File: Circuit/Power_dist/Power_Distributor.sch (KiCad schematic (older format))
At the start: 4 parts, among them CON1 Conn-PCIE-x16, J1 Thruster_Off_Switch

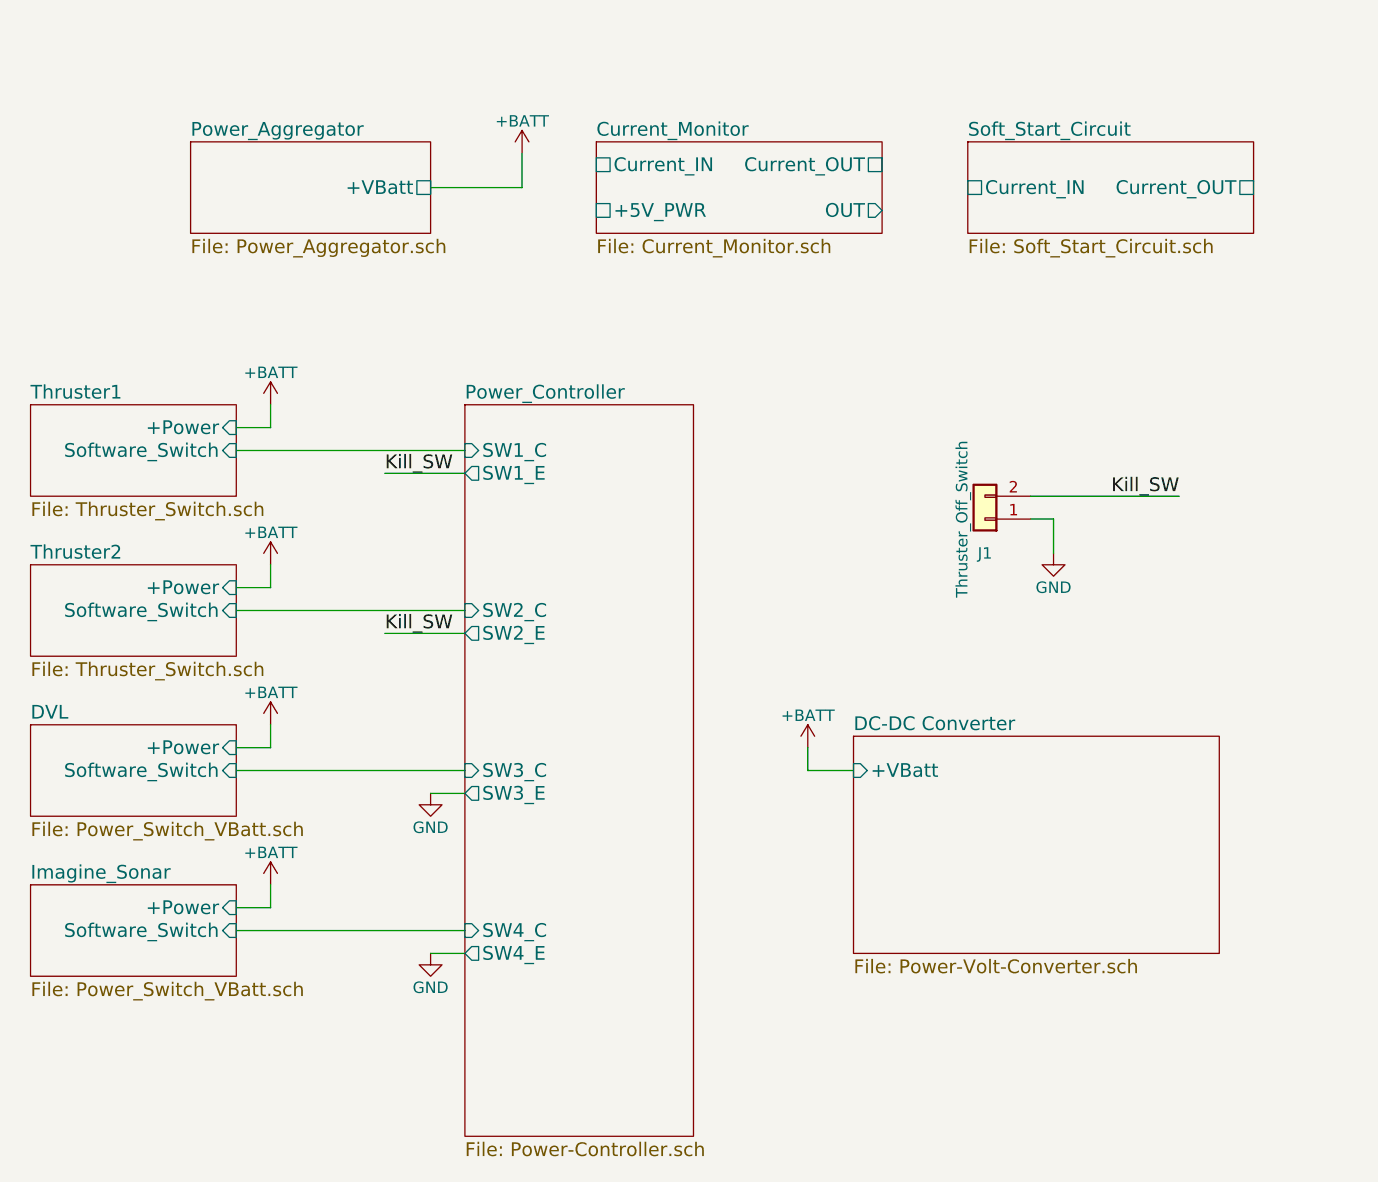
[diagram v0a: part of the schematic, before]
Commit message: added filter to dc-dc converters in Power_dist
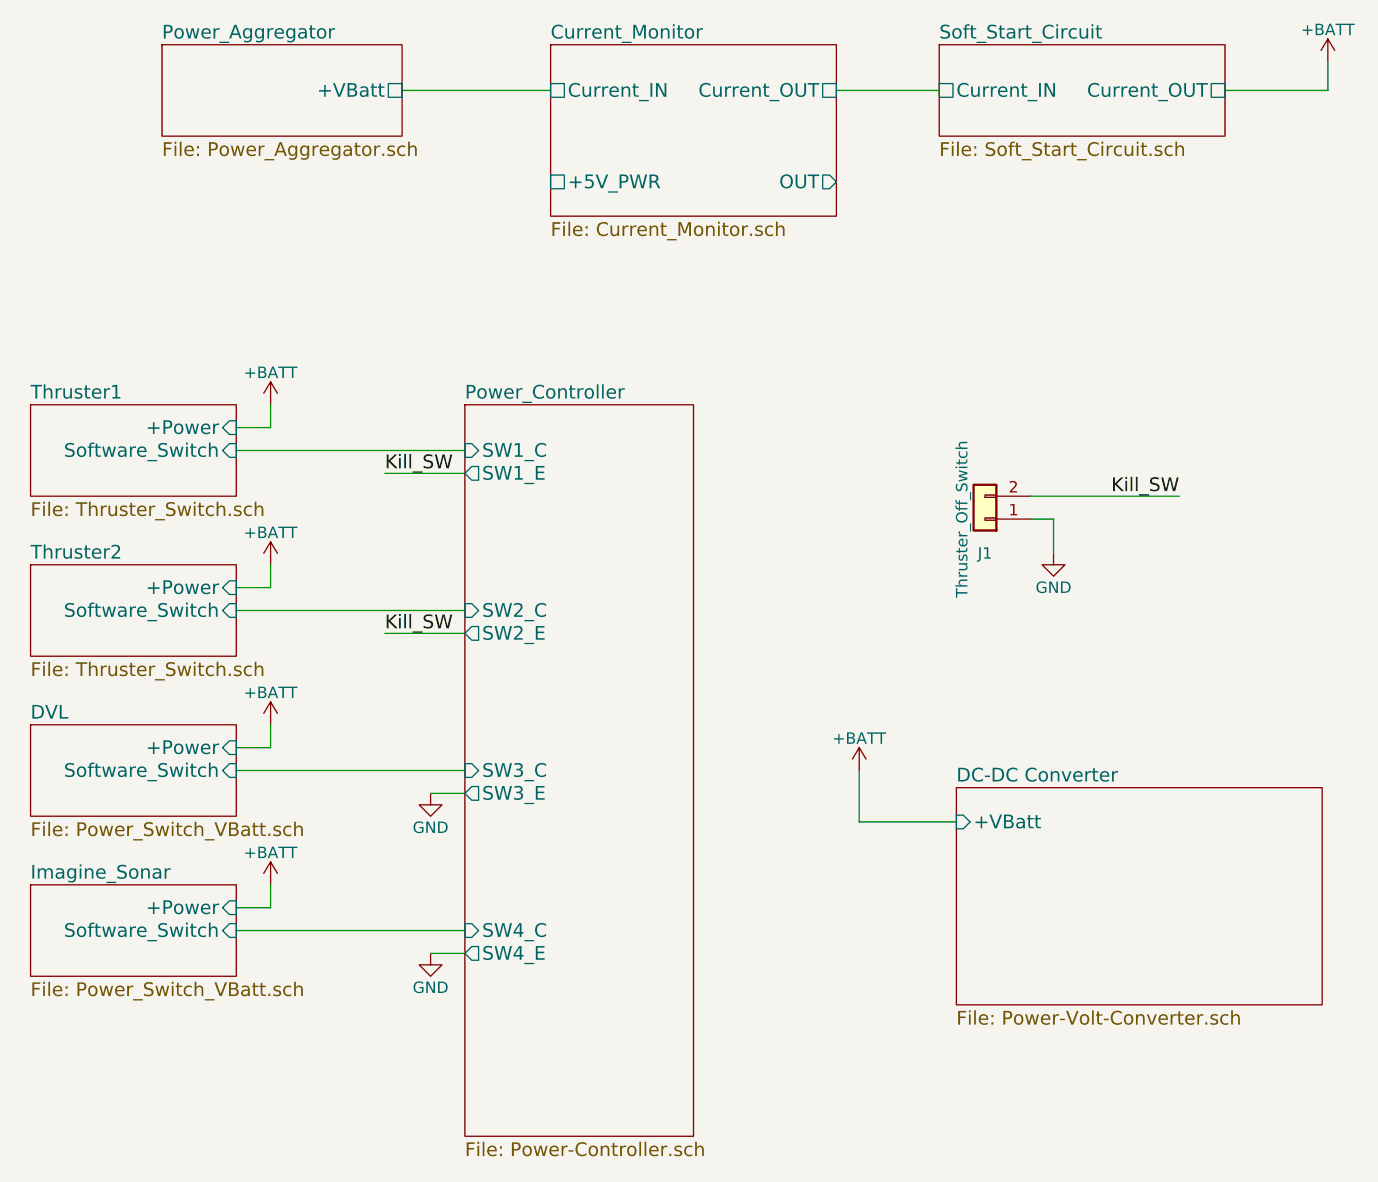
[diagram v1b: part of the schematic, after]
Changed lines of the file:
@@
 L +BATT #PWR01
 U 1 1 58E61C00
-P 6700 1450
-F 0 "#PWR01" H 6700 1300 50  0001 C CNN
-F 1 "+BATT" H 6700 1590 50  0000 C CNN
-F 2 "" H 6700 1450 50  0001 C CNN
-F 3 "" H 6700 1450 50  0001 C CNN
-	1    6700 1450
+P 10225 1050
+F 0 "#PWR01" H 10225 900 50  0001 C CNN
+F 1 "+BATT" H 10225 1190 50  0000 C CNN
+F 2 "" H 10225 1050 50  0001 C CNN
+F 3 "" H 10225 1050 50  0001 C CNN
+	1    10225 1050
 	1    0    0    -1
 $EndComp
@@
 $EndComp
 $Sheet
-S 5250 1400 1050 400
-U 58E5E8B2
-F0 "Power_Aggregator" 60
-F1 "Power_Aggregator.sch" 60
-F2 "+VBatt" U R 6300 1600 60
-$EndSheet
-$Sheet
-S 8150 4000 1600 950
+S 8600 4225 1600 950
 U 58E63E65
 F0 "DC-DC Converter" 60
 F1 "Power-Volt-Converter.sch" 60
-F2 "+VBatt" I L 8150 4150 60
+F2 "+VBatt" I L 8600 4375 60
 $EndSheet
 $Comp
 L +BATT #PWR07
 U 1 1 58E67F6C
-P 7950 4050
-F 0 "#PWR07" H 7950 3900 50  0001 C CNN
-F 1 "+BATT" H 7950 4190 50  0000 C CNN
-F 2 "" H 7950 4050 50  0001 C CNN
-F 3 "" H 7950 4050 50  0001 C CNN
-	1    7950 4050
+P 8175 4150
+F 0 "#PWR07" H 8175 4000 50  0001 C CNN
+F 1 "+BATT" H 8175 4290 50  0000 C CNN
+F 2 "" H 8175 4150 50  0001 C CNN
+F 3 "" H 8175 4150 50  0001 C CNN
+	1    8175 4150
 	1    0    0    -1
 $EndComp
@@
 Wire Wire Line
 	5600 4750 5600 4650
-Wire Wire Line
-	6300 1600 6700 1600
-Wire Wire Line
-	6700 1600 6700 1450
-Wire Wire Line
-	8150 4150 7950 4150
-Wire Wire Line
-	7950 4150 7950 4050
 Wire Wire Line
 	5450 4850 6450 4850
@@
 $EndSheet
 $Sheet
-S 7025 1400 1250 400
+S 6825 975  1250 750
 U 5B4C0CAC
 F0 "Current_Monitor" 60
 F1 "Current_Monitor.sch" 60
-F2 "Current_IN" U L 7025 1500 60
-F3 "Current_OUT" U R 8275 1500 60
-F4 "OUT" O R 8275 1700 60
-F5 "+5V_PWR" U L 7025 1700 60
+F2 "Current_IN" U L 6825 1175 60
+F3 "Current_OUT" U R 8075 1175 60
+F4 "OUT" O R 8075 1575 60
+F5 "+5V_PWR" U L 6825 1575 60
 $EndSheet
 $Sheet
-S 8650 1400 1250 400
+S 8525 975  1250 400
 U 5B4C624E
 F0 "Soft_Start_Circuit" 60
 F1 "Soft_Start_Circuit.sch" 60
-F2 "Current_IN" U L 8650 1600 60
-F3 "Current_OUT" U R 9900 1600 60
+F2 "Current_IN" U L 8525 1175 60
+F3 "Current_OUT" U R 9775 1175 60
 $EndSheet
+$Sheet
+S 5125 975  1050 400
+U 58E5E8B2
+F0 "Power_Aggregator" 60
+F1 "Power_Aggregator.sch" 60
+F2 "+VBatt" U R 6175 1175 60
+$EndSheet
+Wire Wire Line
+	6825 1175 6175 1175
+Wire Wire Line
+	8075 1175 8525 1175
+Wire Wire Line
+	9775 1175 10225 1175
+Wire Wire Line
+	10225 1175 10225 1050
+Wire Wire Line
+	8175 4375 8600 4375
+Wire Wire Line
+	8175 4375 8175 4150
 $EndSCHEMATC

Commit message: added +5v voltage regulator on battery side of Power_dist
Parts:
- added C?: 0.33uF, symbol C_Small
- added C?: 0.1uF, symbol C_Small
- added R?: 0, symbol R
- added U?: L78L05_SOT89, TO_SOT_Packages_SMD:SOT89-3_Housing, symbol L78L05_SOT89
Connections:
- net labels added: +5VP
- wire segments 57 -> 74
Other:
- moved on the sheet: J1
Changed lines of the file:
@@
 L +BATT #PWR01
 U 1 1 58E61C00
-P 10225 1050
-F 0 "#PWR01" H 10225 900 50  0001 C CNN
-F 1 "+BATT" H 10225 1190 50  0000 C CNN
-F 2 "" H 10225 1050 50  0001 C CNN
-F 3 "" H 10225 1050 50  0001 C CNN
-	1    10225 1050
+P 10075 1025
+F 0 "#PWR01" H 10075 875 50  0001 C CNN
+F 1 "+BATT" H 10075 1165 50  0000 C CNN
+F 2 "" H 10075 1025 50  0001 C CNN
+F 3 "" H 10075 1025 50  0001 C CNN
+	1    10075 1025
 	1    0    0    -1
 $EndComp
@@
 L Conn_01x02 J1
 U 1 1 58E6ABEA
-P 8725 3050
-F 0 "J1" H 8725 3200 50  0000 C CNN
-F 1 "Thruster_Off_Switch" V 8825 3050 50  0000 C CNN
-F 2 "Pin_Headers:Pin_Header_Straight_1x02_Pitch2.54mm" H 8725 3050 50  0001 C CNN
-F 3 "" H 8725 3050 50  0001 C CNN
-	1    8725 3050
+P 8725 3225
+F 0 "J1" H 8725 3375 50  0000 C CNN
+F 1 "Thruster_Off_Switch" V 8825 3225 50  0000 C CNN
+F 2 "Pin_Headers:Pin_Header_Straight_1x02_Pitch2.54mm" H 8725 3225 50  0001 C CNN
+F 3 "" H 8725 3225 50  0001 C CNN
+	1    8725 3225
 	-1   0    0    1
 $EndComp
-Text Label 9575 2950 2    60   ~ 0
+Text Label 9575 3125 2    60   ~ 0
 Kill_SW
 $Comp
 L GND #PWR02
 U 1 1 58E6E6F3
-P 9025 3200
-F 0 "#PWR02" H 9025 2950 50  0001 C CNN
-F 1 "GND" H 9025 3050 50  0000 C CNN
-F 2 "" H 9025 3200 50  0001 C CNN
-F 3 "" H 9025 3200 50  0001 C CNN
-	1    9025 3200
+P 9025 3375
+F 0 "#PWR02" H 9025 3125 50  0001 C CNN
+F 1 "GND" H 9025 3225 50  0000 C CNN
+F 2 "" H 9025 3375 50  0001 C CNN
+F 3 "" H 9025 3375 50  0001 C CNN
+	1    9025 3375
 	1    0    0    -1
 $EndComp
@@
 F0 "DC-DC Converter" 60
 F1 "Power-Volt-Converter.sch" 60
-F2 "+VBatt" I L 8600 4375 60
+F2 "+VBatt" U L 8600 4375 60
+F3 "+12V" U L 8600 4850 60
+F4 "+5V" U L 8600 5000 60
 $EndSheet
 $Comp
@@
 	1    0    0    -1
 $EndComp
-Wire Wire Line
-	8925 3050 9025 3050
-Wire Wire Line
-	9025 3050 9025 3200
-Wire Wire Line
-	9575 2950 8925 2950
-Wire Wire Line
-	5600 2550 5600 2650
-Wire Wire Line
-	5600 2650 5450 2650
-Wire Wire Line
-	5600 3250 5600 3350
-Wire Wire Line
-	5600 3350 5450 3350
-Wire Wire Line
-	5600 3950 5600 4050
-Wire Wire Line
-	5600 4050 5450 4050
-Wire Wire Line
-	5450 4750 5600 4750
-Wire Wire Line
-	5600 4750 5600 4650
-Wire Wire Line
-	5450 4850 6450 4850
-Wire Wire Line
-	6450 4150 5450 4150
-Wire Wire Line
-	5450 3450 6450 3450
-Wire Wire Line
-	6450 2750 5450 2750
-Wire Wire Line
-	6100 2850 6450 2850
-Wire Wire Line
-	6100 3550 6450 3550
-Wire Wire Line
-	6300 4250 6450 4250
-Wire Wire Line
-	6450 4950 6300 4950
-Wire Wire Line
-	1950 2750 1450 2750
-Wire Wire Line
-	1950 2650 1450 2650
-Wire Wire Line
-	650  2150 1950 2150
-Wire Wire Line
-	3500 2150 3100 2150
-Wire Wire Line
-	3500 2050 3500 2150
-Wire Wire Line
-	3100 2050 3500 2050
-Connection ~ 3500 2050
-Wire Wire Line
-	1950 1950 1450 1950
-Wire Wire Line
-	1450 1950 1450 1900
-Wire Wire Line
-	1450 1450 1950 1450
-Wire Wire Line
-	1450 1150 1450 1450
-Wire Wire Line
-	1950 1250 1450 1250
-Connection ~ 1450 1250
-Wire Wire Line
-	1950 1350 1450 1350
-Connection ~ 1450 1350
 $Comp
 L +12V #PWR013
@@
 	1    0    0    -1
 $EndComp
-Wire Wire Line
-	1850 1850 1950 1850
 $Comp
 L GNDD #PWR015
@@
 	1    0    0    -1
 $EndComp
-Wire Wire Line
-	1050 1550 1950 1550
-Wire Wire Line
-	3100 1350 3500 1350
-Wire Wire Line
-	3500 1350 3500 1250
-Wire Wire Line
-	3100 1450 3900 1450
-Wire Wire Line
-	3900 1450 3900 1250
 $Comp
 L +BATT #PWR017
@@
 	1    0    0    -1
 $EndComp
-Wire Wire Line
-	1850 1850 1850 1650
-Wire Wire Line
-	1850 1650 1650 1650
-Wire Wire Line
-	1650 1650 1650 1700
 $Comp
 L GND #PWR018
@@
 	1    0    0    -1
 $EndComp
-Wire Wire Line
-	1950 2850 1450 2850
-Wire Wire Line
-	1450 2850 1450 2900
 $Comp
 L GNDREF #PWR019
@@
 	1    0    0    -1
 $EndComp
-Wire Wire Line
-	1950 2550 1050 2550
-Wire Wire Line
-	1950 3050 1050 3050
-Wire Wire Line
-	3100 2450 3500 2450
-Wire Wire Line
-	3100 2750 3500 2750
-Wire Wire Line
-	3500 3050 3100 3050
-Wire Wire Line
-	3500 1550 3100 1550
 $Comp
 L LED_Small D7
@@
 	1    0    0    -1
 $EndComp
-Wire Wire Line
-	800  2250 800  2150
-Connection ~ 800  2150
-Wire Wire Line
-	800  2450 800  2550
-Wire Wire Line
-	800  2850 800  2950
 Text GLabel 1450 2650 0    60   Input ~ 0
 D+
@@
 F2 "+VBatt" U R 6175 1175 60
 $EndSheet
+$Comp
+L +12V #PWR?
+U 1 1 5B4E546A
+P 8350 4725
+F 0 "#PWR?" H 8350 4575 50  0001 C CNN
+F 1 "+12V" H 8350 4865 50  0000 C CNN
+F 2 "" H 8350 4725 50  0001 C CNN
+F 3 "" H 8350 4725 50  0001 C CNN
+	1    8350 4725
+	1    0    0    -1
+$EndComp
+$Comp
+L +5V #PWR?
+U 1 1 5B4E56B8
+P 8175 4825
+F 0 "#PWR?" H 8175 4675 50  0001 C CNN
+F 1 "+5V" H 8175 4965 50  0000 C CNN
+F 2 "" H 8175 4825 50  0001 C CNN
+F 3 "" H 8175 4825 50  0001 C CNN
+	1    8175 4825
+	1    0    0    -1
+$EndComp
+$Comp
+L L78L05_SOT89 U?
+U 1 1 5B4F178E
+P 9450 2175
+F 0 "U?" H 9300 2300 50  0000 C CNN
+F 1 "L78L05_SOT89" H 9450 2300 50  0000 L CNN
+F 2 "TO_SOT_Packages_SMD:SOT89-3_Housing" H 9450 2375 50  0001 C CIN
+F 3 "" H 9450 2125 50  0001 C CNN
+	1    9450 2175
+	1    0    0    -1
+$EndComp
+$Comp
+L +BATT #PWR?
+U 1 1 5B4F33C0
+P 8400 2050
+F 0 "#PWR?" H 8400 1900 50  0001 C CNN
+F 1 "+BATT" H 8400 2190 50  0000 C CNN
+F 2 "" H 8400 2050 50  0001 C CNN
+F 3 "" H 8400 2050 50  0001 C CNN
+	1    8400 2050
+	1    0    0    -1
+$EndComp
+$Comp
+L GND #PWR?
+U 1 1 5B4F9079
+P 9450 2575
+F 0 "#PWR?" H 9450 2325 50  0001 C CNN
+F 1 "GND" H 9450 2425 50  0000 C CNN
+F 2 "" H 9450 2575 50  0001 C CNN
+F 3 "" H 9450 2575 50  0001 C CNN
+	1    9450 2575
+	1    0    0    -1
+$EndComp
+$Comp
+L C_Small C?
+U 1 1 5B503C5F
+P 8975 2350
+F 0 "C?" H 8985 2420 50  0000 L CNN
+F 1 "0.33uF" H 8985 2270 50  0000 L CNN
+F 2 "" H 8975 2350 50  0001 C CNN
+F 3 "" H 8975 2350 50  0001 C CNN
+	1    8975 2350
+	1    0    0    -1
+$EndComp
+$Comp
+L C_Small C?
+U 1 1 5B5057E1
+P 9925 2350
+F 0 "C?" H 9935 2420 50  0000 L CNN
+F 1 "0.1uF" H 9935 2270 50  0000 L CNN
+F 2 "" H 9925 2350 50  0001 C CNN
+F 3 "" H 9925 2350 50  0001 C CNN
+	1    9925 2350
+	1    0    0    -1
+$EndComp
+$Comp
+L +5VP #PWR?
+U 1 1 5B507F80
+P 10175 2050
+F 0 "#PWR?" H 10175 1900 50  0001 C CNN
+F 1 "+5VP" H 10175 2190 50  0000 C CNN
+F 2 "" H 10175 2050 50  0001 C CNN
+F 3 "" H 10175 2050 50  0001 C CNN
+	1    10175 2050
+	1    0    0    -1
+$EndComp
+$Comp
+L +5VP #PWR?
+U 1 1 5B50B27D
+P 6650 1500
+F 0 "#PWR?" H 6650 1350 50  0001 C CNN
+F 1 "+5VP" H 6650 1640 50  0000 C CNN
+F 2 "" H 6650 1500 50  0001 C CNN
+F 3 "" H 6650 1500 50  0001 C CNN
+	1    6650 1500
+	1    0    0    -1
+$EndComp
+$Comp
+L R R?
+U 1 1 5B52DE29
+P 8675 2175
+F 0 "R?" V 8755 2175 50  0000 C CNN
+F 1 "0" V 8675 2175 50  0000 C CNN
+F 2 "" V 8605 2175 50  0001 C CNN
+F 3 "" H 8675 2175 50  0001 C CNN
+	1    8675 2175
+	0    1    1    0
+$EndComp
+Wire Wire Line
+	8925 3225 9025 3225
+Wire Wire Line
+	9025 3225 9025 3375
+Wire Wire Line
+	9575 3125 8925 3125
+Wire Wire Line
+	5600 2550 5600 2650
+Wire Wire Line
+	5600 2650 5450 2650
+Wire Wire Line
+	5600 3250 5600 3350
+Wire Wire Line
+	5600 3350 5450 3350
+Wire Wire Line
+	5600 3950 5600 4050
+Wire Wire Line
+	5600 4050 5450 4050
+Wire Wire Line
+	5450 4750 5600 4750
+Wire Wire Line
+	5600 4750 5600 4650
+Wire Wire Line
+	5450 4850 6450 4850
+Wire Wire Line
+	6450 4150 5450 4150
+Wire Wire Line
+	5450 3450 6450 3450
+Wire Wire Line
+	6450 2750 5450 2750
+Wire Wire Line
+	6100 2850 6450 2850
+Wire Wire Line
+	6100 3550 6450 3550
+Wire Wire Line
+	6300 4250 6450 4250
+Wire Wire Line
+	6450 4950 6300 4950
+Wire Wire Line
+	1950 2750 1450 2750
+Wire Wire Line
+	1950 2650 1450 2650
+Wire Wire Line
+	650  2150 1950 2150
+Wire Wire Line
+	3500 2150 3100 2150
+Wire Wire Line
+	3500 2050 3500 2150
+Wire Wire Line
+	3100 2050 3500 2050
+Connection ~ 3500 2050
+Wire Wire Line
+	1950 1950 1450 1950
+Wire Wire Line
+	1450 1950 1450 1900
+Wire Wire Line
+	1450 1450 1950 1450
+Wire Wire Line
+	1450 1150 1450 1450
+Wire Wire Line
+	1950 1250 1450 1250
+Connection ~ 1450 1250
+Wire Wire Line
+	1950 1350 1450 1350
+Connection ~ 1450 1350
+Wire Wire Line
+	1850 1850 1950 1850
+Wire Wire Line
+	1050 1550 1950 1550
+Wire Wire Line
+	3100 1350 3500 1350
+Wire Wire Line
+	3500 1350 3500 1250
+Wire Wire Line
+	3100 1450 3900 1450
+Wire Wire Line
+	3900 1450 3900 1250
+Wire Wire Line
+	1850 1850 1850 1650
+Wire Wire Line
+	1850 1650 1650 1650
+Wire Wire Line
+	1650 1650 1650 1700
+Wire Wire Line
+	1950 2850 1450 2850
+Wire Wire Line
+	1450 2850 1450 2900
+Wire Wire Line
+	1950 2550 1050 2550
+Wire Wire Line
+	1950 3050 1050 3050
+Wire Wire Line
+	3100 2450 3500 2450
+Wire Wire Line
+	3100 2750 3500 2750
+Wire Wire Line
+	3500 3050 3100 3050
+Wire Wire Line
+	3500 1550 3100 1550
+Wire Wire Line
+	800  2250 800  2150
+Connection ~ 800  2150
+Wire Wire Line
+	800  2450 800  2550
+Wire Wire Line
+	800  2850 800  2950
 Wire Wire Line
 	6825 1175 6175 1175
@@
 	8075 1175 8525 1175
 Wire Wire Line
-	9775 1175 10225 1175
-Wire Wire Line
-	10225 1175 10225 1050
-Wire Wire Line
 	8175 4375 8600 4375
 Wire Wire Line
 	8175 4375 8175 4150
+Wire Wire Line
+	8350 4725 8350 4850
+Wire Wire Line
+	8350 4850 8600 4850
+Wire Wire Line
+	8175 4825 8175 5000
+Wire Wire Line
+	8175 5000 8600 5000
+Wire Wire Line
+	8400 2050 8400 2175
+Wire Wire Line
+	10075 1025 10075 1175
+Wire Wire Line
+	10075 1175 9775 1175
+Wire Wire Line
+	9450 2575 9450 2475
+Connection ~ 9450 2525
+Wire Wire Line
+	10175 2175 10175 2050
+Wire Wire Line
+	6650 1500 6650 1575
+Wire Wire Line
+	6650 1575 6825 1575
+Wire Wire Line
+	8400 2175 8525 2175
+Wire Wire Line
+	8825 2175 9150 2175
+Wire Wire Line
+	8975 2175 8975 2250
+Connection ~ 8975 2175
+Wire Wire Line
+	8975 2525 8975 2450
+Wire Wire Line
+	8975 2525 9925 2525
+Wire Wire Line
+	9750 2175 10175 2175
+Wire Wire Line
+	9925 2250 9925 2175
+Connection ~ 9925 2175
+Wire Wire Line
+	9925 2525 9925 2450
 $EndSCHEMATC

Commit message: refactor Power_dist
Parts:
- added D13: BATT2_LED, LEDs:LED_0603_HandSoldering, symbol D_Small
- added D14: BATT_LED, LEDs:LED_0603_HandSoldering, symbol D_Small
- added D6: BATT1_LED, LEDs:LED_0603_HandSoldering, symbol D_Small
- added D?: PWR_LED, LEDs:LED_0603_HandSoldering, symbol D_Small
- added P16: BATT1, zeabus:XT60, symbol XT60
- added P17: BATT2, zeabus:XT60, symbol XT60
- added R11, R12: 10k, Resistors_SMD:R_0603_HandSoldering, symbol R
- added R29, R?: 10k, symbol R
- C? (x2): footprint (none) -> Capacitors_SMD:C_0603_HandSoldering
- D7: value LED_Small -> VBUS_LED
- JP3: renamed from J1; symbol Conn_01x02 -> Jumper
- R?: footprint (none) -> Resistors_SMD:R_0603_HandSoldering
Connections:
- net labels added: GNDPWR, KILL_SWITCH
- net labels removed: GND, Kill_SW
- wire segments 74 -> 102
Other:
- moved on the sheet: C?, CON1A, D7, R10, R?

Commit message: changed pmos in Power_Switch_VBatt of Power_dist to STR2P3LLH6
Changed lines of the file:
@@
 F0 "Thruster2" 60
 F1 "Thruster_Switch.sch" 60
-F2 "+Power" I R 5450 3750 60
-F3 "Software_Switch" I R 5450 3850 60
-$EndSheet
-$Sheet
-S 4550 4350 900  400
-U 58E51F99
-F0 "DVL" 60
-F1 "Power_Switch_VBatt.sch" 60
-F2 "+Power" I R 5450 4450 60
-F3 "Software_Switch" I R 5450 4550 60
+F2 "+PWR" U R 5450 3750 60
+F3 "Software_SW" U R 5450 3850 60
 $EndSheet
 $Sheet
@@
 F0 "Imagine_Sonar" 60
 F1 "Power_Switch_VBatt.sch" 60
-F2 "+Power" I R 5450 5150 60
-F3 "Software_Switch" I R 5450 5250 60
+F2 "+PWR" U R 5450 5150 60
+F3 "Software_SW" U R 5450 5250 60
 $EndSheet
 $Comp
@@
 F0 "Thruster1" 60
 F1 "Thruster_Switch.sch" 60
-F2 "+Power" I R 5450 3050 60
-F3 "Software_Switch" I R 5450 3150 60
+F2 "+PWR" U R 5450 3050 60
+F3 "Software_SW" U R 5450 3150 60
 $EndSheet
 $Comp
@@
 Wire Wire Line
 	6325 3950 6450 3950
+$Sheet
+S 4550 4350 900  400
+U 58E51F99
+F0 "DVL" 60
+F1 "Power_Switch_VBatt.sch" 60
+F2 "+PWR" U R 5450 4450 60
+F3 "Software_SW" U R 5450 4550 60
+$EndSheet
 $EndSCHEMATC

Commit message: added Thruster_Switch3 to Power_dist
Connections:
- wire segments 102 -> 103
